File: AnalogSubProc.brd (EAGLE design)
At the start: 12.5 x 8.3 mm, 19 parts, among them IC3 LTC6087

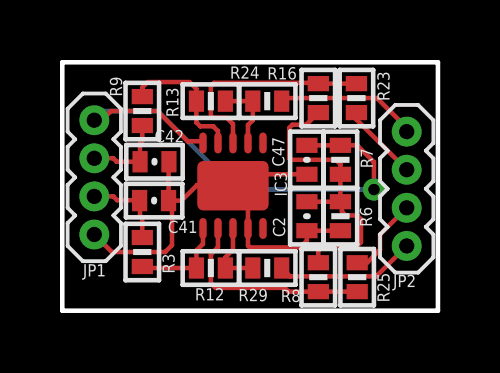
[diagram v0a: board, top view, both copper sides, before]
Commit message: Smaller board succesfully routed.
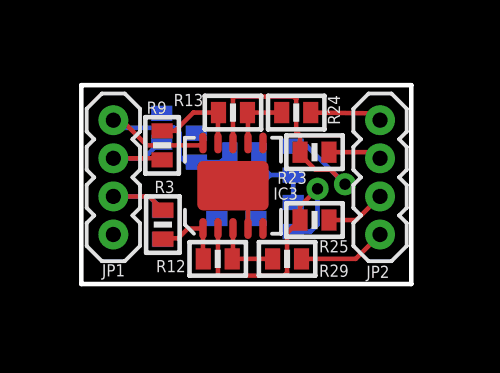
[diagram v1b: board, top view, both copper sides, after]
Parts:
- moved C47 3.71 mm to (5.94, 5.56), flipped to the bottom, turned to 90 degrees
- moved R7 3.21 mm to (7.54, 5.38), flipped to the bottom, turned to 0 degrees
- moved C2 3.02 mm to (6.63, 3.68), flipped to the bottom
- moved R6 2.85 mm to (7.92, 3.68), flipped to the bottom
- moved R25 2.38 mm to (9.88, 3.15), turned to 0 degrees
- moved R23 2.28 mm to (9.88, 5.41), turned to 0 degrees
- moved R16 2.25 mm to (9.17, 5.13), flipped to the bottom
- moved R8 2.17 mm to (9.17, 3.25), flipped to the bottom
- moved R9 1.32 mm to (4.80, 5.64)
- moved C42 1.16 mm to (4.79, 6.22), flipped to the bottom, turned to 90 degrees
- moved R3 1.14 mm to (4.83, 3.00)
- moved R24 1.04 mm to (9.27, 6.73)
- moved JP2 0.97 mm to (12.1, 6.48)
- moved C41 0.86 mm to (4.81, 2.98), flipped to the bottom, turned to 270 degrees
- moved R13 0.83 mm to (7.16, 6.73)
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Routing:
- net GND: track 16.5 -> 2.17 mm
- net 3.3V: track 18.3 -> 8.46 mm, vias 1 -> 0
- net V_REF: track 10.2 -> 4.62 mm
- net N$31: track 6.92 -> 9.45 mm, vias 0 -> 1
- net MOTOR_B_OUT2: track 4.75 -> 2.41 mm
- net N$23: track 7.64 -> 9.72 mm, vias 0 -> 1
- net MOTOR_A_OUT1: track 4.70 -> 2.95 mm
- net N$37: track 4.86 -> 3.15 mm
- net MOTOR_A_BEMF: track 2.84 -> 3.69 mm
- net MOTOR_B_OUT1: track 2.60 -> 1.79 mm
- net N$36: track 3.23 -> 2.50 mm
- net MOTOR_B_BEMF: track 2.83 -> 3.51 mm
- net MOTOR_A_OUT2: track 2.71 -> 2.03 mm
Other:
- board size 12.5 x 8.3 mm -> 11 x 6.6 mm
